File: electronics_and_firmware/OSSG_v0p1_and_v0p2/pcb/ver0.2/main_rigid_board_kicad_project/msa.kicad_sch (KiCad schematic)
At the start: 53 parts, among them J1 USB_B_Micro, J2 SWD Prog, SW1 SW_SPST, U1 MCP1702, U2 MCP73831-2-OT, U3 W25Q128JV, U4 RP2040, U5 ‎DMP21D0UT-7‎, Y1 H130B-12.000-20-3050-EXT-TR

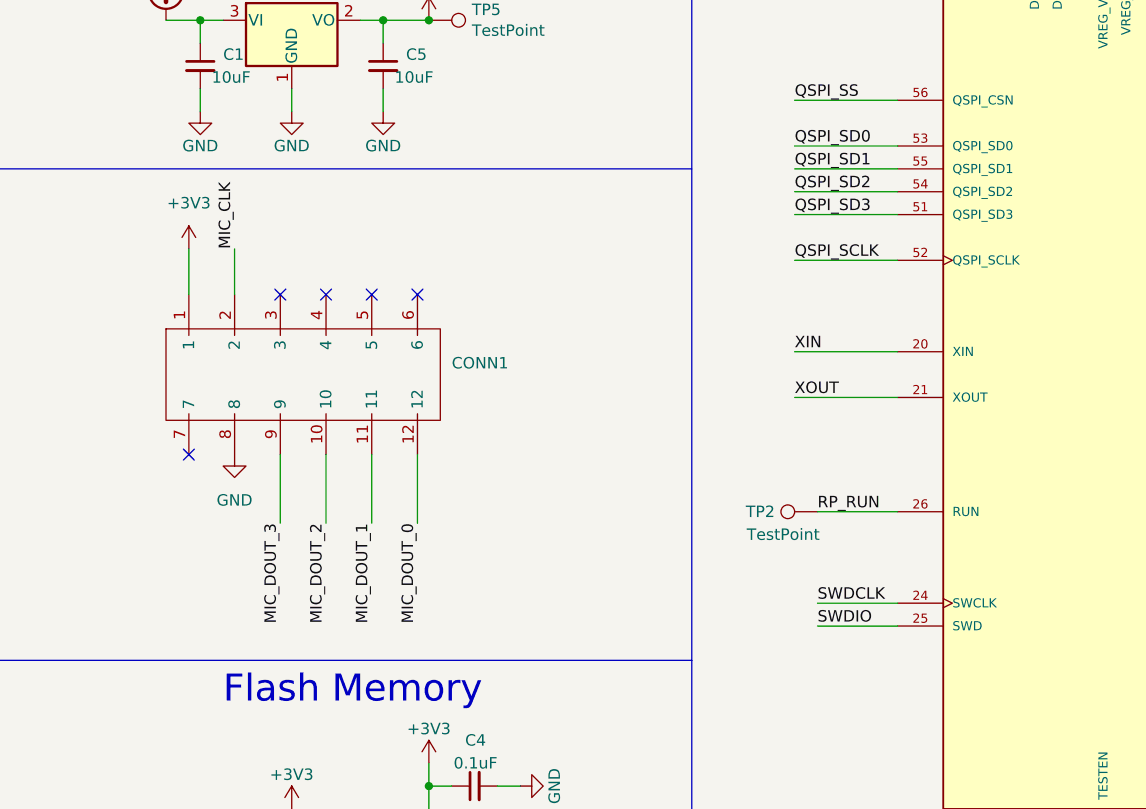
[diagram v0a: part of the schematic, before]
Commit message: fix MSAv0p2 main board pcb connector pinout, fix gerber renders, update README
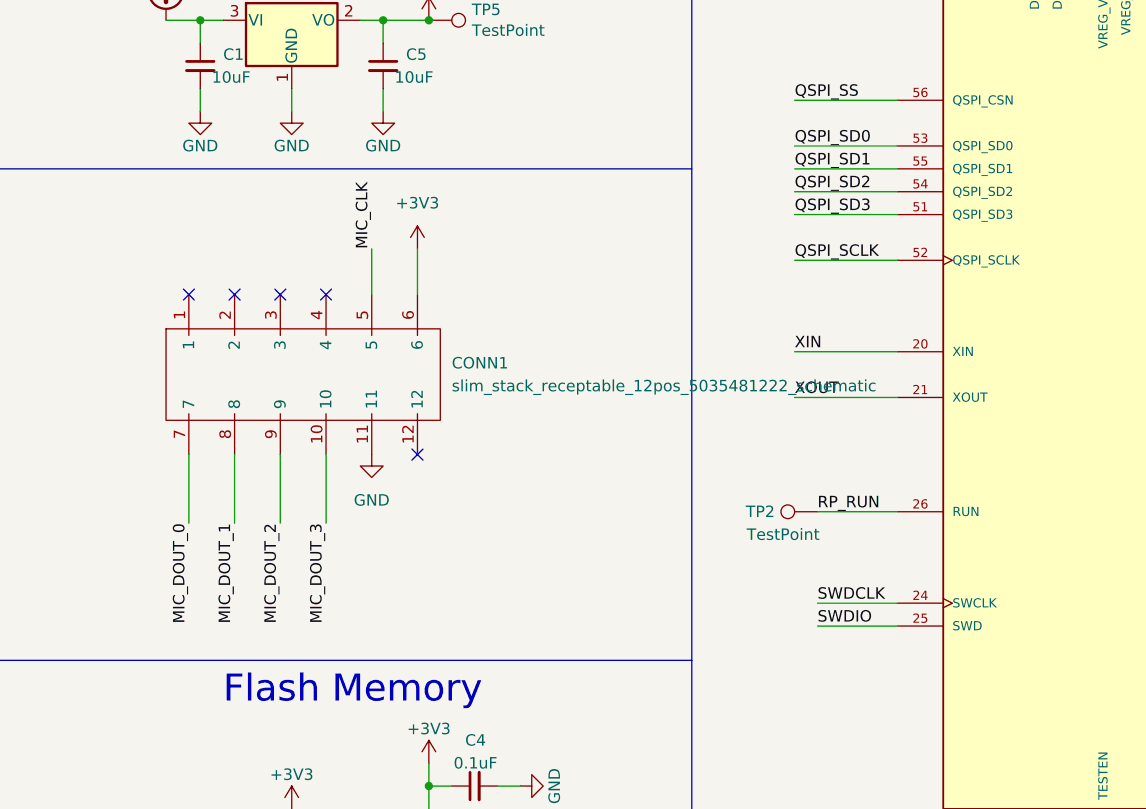
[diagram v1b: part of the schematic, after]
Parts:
- CONN1: value (none) -> slim_stack_receptable_12pos_5035481222_schematic; footprint (none) -> OpenSourceSmartGlasses:slim_stack_molex_RECEPTACLE_5035481222
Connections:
- net +3V3: now also CONN1.6; no longer CONN1.1
- net -BATT: now also CONN1.11; no longer CONN1.8
- net MIC_CLK: now also CONN1.5; no longer CONN1.2
- net MIC_DOUT_0: now also CONN1.7; no longer CONN1.12
- net MIC_DOUT_1: now also CONN1.8; no longer CONN1.11
- net MIC_DOUT_2: now also CONN1.9; no longer CONN1.10
- net MIC_DOUT_3: now also CONN1.10; no longer CONN1.9
